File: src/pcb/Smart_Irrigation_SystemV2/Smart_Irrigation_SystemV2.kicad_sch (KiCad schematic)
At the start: 133 parts, among them CN1 PJ-3136-3A, CN2 PJ-3136-3A, CN3 PJ-3136-3A, CN4 PJ-3136-3A, CN5 PJ-3136-3A, CN6 PJ-3136-3A, J1 USB_C_Receptacle_USB2.0_16P, J10 I2C, J11 I2C, J13 I2C, J14 SolarPanel, J15 I2C, J16 GPIO_Expander, J2 FPC_Connector, J6 I2C, J9 Battary Connection, Q1 MUN5211DW1, Q2 FDN340P, Q3 AO3400A, SW1 IO0 Switch, SW2 EN Switch, SW3 SW_Push, SW4 SW_Push, SW5 SW_Push, SW6 SW_Push, U1 CP2102N-Axx-xQFN28, U10 ADS1115IDGS, U11 PCA9536DP, U2 ESP32-WROOM-32, U3 ADS1115IDGS, U4 DS3231MZ, U5 TLV62568ADRL, U6 SN74LVC245APW, U7 TP4056-42-ESOP8, U8 TPS63001, U9 AT24CS32-SSHM

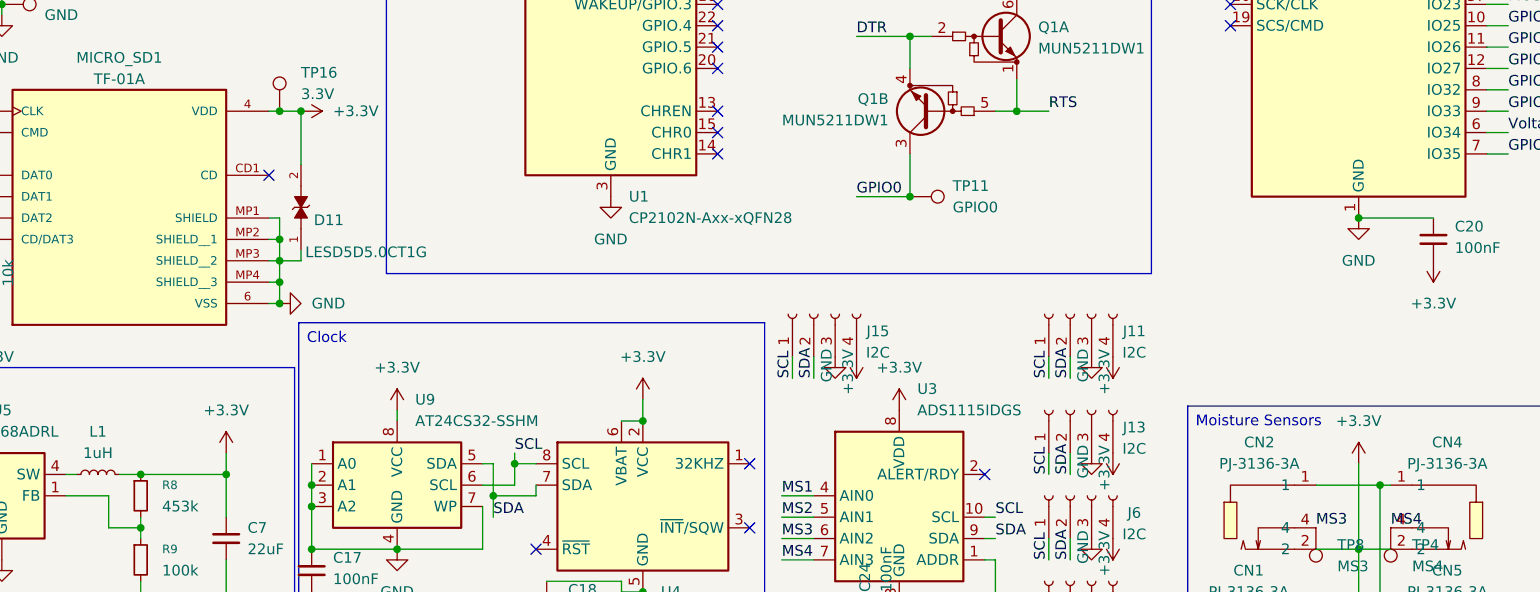
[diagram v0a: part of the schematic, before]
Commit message: solved warnings from drc and menaged silkscreen
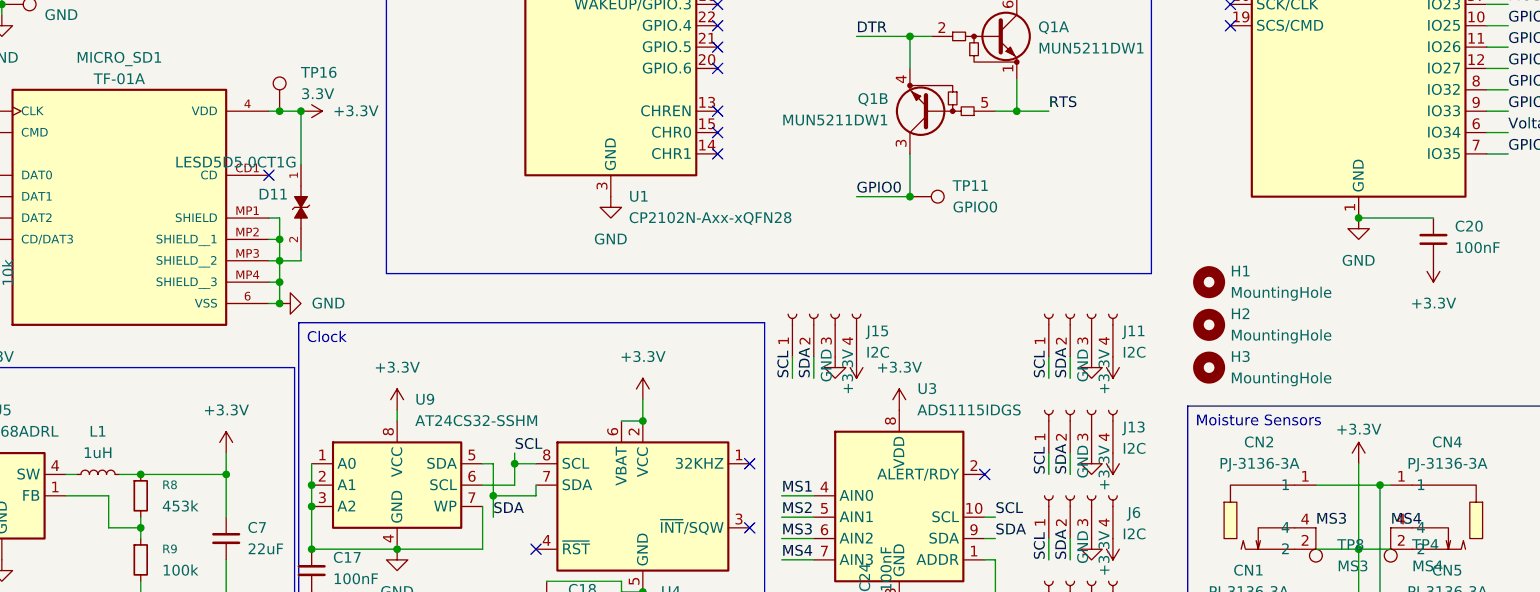
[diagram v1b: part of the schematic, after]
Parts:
- added H1, H2, H3: MountingHole, MountingHole:MountingHole_2.2mm_M2, symbol Mechanical:MountingHole
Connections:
- net +3.3V: now also D11.1; no longer D11.2
- net GND: now also D11.2; no longer D11.1
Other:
- moved on the sheet: D11
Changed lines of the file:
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@@
 	)
 	(symbol
+		(lib_id "Mechanical:MountingHole")
+		(at 173.99 96.52 0)
+		(unit 1)
+		(body_style 1)
+		(exclude_from_sim no)
+		(in_bom no)
+		(on_board yes)
+		(in_pos_files yes)
+		(dnp no)
+		(fields_autoplaced yes)
+		(property "Reference" "H1"
+			(at 176.53 95.2499 0)
+			(show_name no)
+			(do_not_autoplace no)
+			(effects
+				(font
+					(size 1.27 1.27)
+				)
+				(justify left)
+			)
+		)
+		(property "Value" "MountingHole"
+			(at 176.53 97.7899 0)
+			(show_name no)
+			(do_not_autoplace no)
+			(effects
+				(font
+					(size 1.27 1.27)
+				)
+				(justify left)
+			)
+		)
+		(property "Footprint" "MountingHole:MountingHole_2.2mm_M2"
+			(at 173.99 96.52 0)
+			(hide yes)
+			(show_name no)
+			(do_not_autoplace no)
+			(effects
+				(font
+					(size 1.27 1.27)
+				)
+			)
+		)
+		(property "Datasheet" ""
+			(at 173.99 96.52 0)
+			(hide yes)
+			(show_name no)
+			(do_not_autoplace no)
+			(effects
+				(font
+					(size 1.27 1.27)
+				)
+			)
+		)
+		(property "Description" "Mounting Hole without connection"
+			(at 173.99 96.52 0)
+			(hide yes)
+			(show_name no)
+			(do_not_autoplace no)
+			(effects
+				(font
+					(size 1.27 1.27)
+				)
+			)
+		)
+		(instances
+			(project "Smart_Irrigation_SystemV2"
+				(path "/53cd4412-b596-463c-8d76-f5cd1a4639a9"
+					(reference "H1")
+					(unit 1)
+				)
+			)
+		)
+	)
+	(symbol
 		(lib_id "Device:C_Small")
 		(at 208.28 171.45 0)
@@
 	(symbol
 		(lib_id "LESD5D5.0CT1G:LESD5D5.0CT1G")
-		(at 66.04 87.63 270)
+		(at 66.04 87.63 90)
 		(mirror x)
 		(unit 1)
@@
 		(dnp no)
 		(property "Reference" "D11"
-			(at 67.564 89.154 90)
+			(at 64.516 86.106 90)
 			(show_name no)
 			(do_not_autoplace no)
@@
 		)
 		(property "Value" "LESD5D5.0CT1G"
-			(at 66.548 92.964 90)
+			(at 65.532 82.296 90)
 			(show_name no)
 			(do_not_autoplace no)
@@
 		(in_pos_files yes)
 		(dnp no)
-		(fields_autoplaced yes)
 		(property "Reference" "#PWR069"
 			(at 191.77 121.92 0)
@@
 		)
 		(property "Value" "+3.3V"
-			(at 191.77 113.03 0)
+			(at 191.77 114.046 0)
 			(show_name no)
 			(do_not_autoplace no)
@@
 	)
 	(symbol
+		(lib_id "Mechanical:MountingHole")
+		(at 173.99 106.68 0)
+		(unit 1)
+		(body_style 1)
+		(exclude_from_sim no)
+		(in_bom no)
+		(on_board yes)
+		(in_pos_files yes)
+		(dnp no)
+		(fields_autoplaced yes)
+		(property "Reference" "H3"
+			(at 176.53 105.4099 0)
+			(show_name no)
+			(do_not_autoplace no)
+			(effects
+				(font
+					(size 1.27 1.27)
+				)
+				(justify left)
+			)
+		)
+		(property "Value" "MountingHole"
+			(at 176.53 107.9499 0)
+			(show_name no)
+			(do_not_autoplace no)
+			(effects
+				(font
+					(size 1.27 1.27)
+				)
+				(justify left)
+			)
+		)
+		(property "Footprint" "MountingHole:MountingHole_2.2mm_M2"
+			(at 173.99 106.68 0)
+			(hide yes)
+			(show_name no)
+			(do_not_autoplace no)
+			(effects
+				(font
+					(size 1.27 1.27)
+				)
+			)
+		)
+		(property "Datasheet" ""
+			(at 173.99 106.68 0)
+			(hide yes)
+			(show_name no)
+			(do_not_autoplace no)
+			(effects
+				(font
+					(size 1.27 1.27)
+				)
+			)
+		)
+		(property "Description" "Mounting Hole without connection"
+			(at 173.99 106.68 0)
+			(hide yes)
+			(show_name no)
+			(do_not_autoplace no)
+			(effects
+				(font
+					(size 1.27 1.27)
+				)
+			)
+		)
+		(instances
+			(project "Smart_Irrigation_SystemV2"
+				(path "/53cd4412-b596-463c-8d76-f5cd1a4639a9"
+					(reference "H3")
+					(unit 1)
+				)
+			)
+		)
+	)
+	(symbol
 		(lib_id "Device:R_Small")
 		(at 238.76 46.99 180)
@@
 					(unit 1)
 				)
+			)
+		)
+	)
+	(symbol
+		(lib_id "Mechanical:MountingHole")
+		(at 173.99 101.6 0)
+		(unit 1)
+		(body_style 1)
+		(exclude_from_sim no)
+		(in_bom no)
+		(on_board yes)
+		(in_pos_files yes)
+		(dnp no)
+		(fields_autoplaced yes)
+		(property "Reference" "H2"
+			(at 176.53 100.3299 0)
+			(show_name no)
+			(do_not_autoplace no)
+			(effects
+				(font
+					(size 1.27 1.27)
+				)
+				(justify left)
+			)
+		)
+		(property "Value" "MountingHole"
+			(at 176.53 102.8699 0)
+			(show_name no)
+			(do_not_autoplace no)
+			(effects
+				(font
+					(size 1.27 1.27)
+				)
+				(justify left)
+			)
+		)
+		(property "Footprint" "MountingHole:MountingHole_2.2mm_M2"
+			(at 173.99 101.6 0)
+			(hide yes)
+			(show_name no)
+			(do_not_autoplace no)
+			(effects
+				(font
+					(size 1.27 1.27)
+				)
+			)
+		)
+		(property "Datasheet" ""
+			(at 173.99 101.6 0)
+			(hide yes)
+			(show_name no)
+			(do_not_autoplace no)
+			(effects
+				(font
+					(size 1.27 1.27)
+				)
+			)
+		)
+		(property "Description" "Mounting Hole without connection"
+			(at 173.99 101.6 0)
+			(hide yes)
+			(show_name no)
+			(do_not_autoplace no)
+			(effects
+				(font
+					(size 1.27 1.27)
+				)
+			)
+		)
+		(instances
+			(project "Smart_Irrigation_SystemV2"
+				(path "/53cd4412-b596-463c-8d76-f5cd1a4639a9"
+					(reference "H2")
+					(unit 1)
+				)

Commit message: first gerber files, last polish
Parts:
- CN1, CN2, CN3, CN4, CN5, CN6: JLCPCB Part Number (none) -> C707248
- D10: JLCPCB Part Number C5355496 -> C513277
- U8: footprint C28060:VSON-10_L3.0-W3.0-P0.50-TL-EP_TPS62410DRCR -> Package_TO_SOT_SMD:SOT-23-5
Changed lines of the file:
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@@
 			)
 		)
+		(property "JLCPCB Part Number" "C707248"
+			(at 181.61 153.67 0)
+			(hide yes)
+			(show_name no)
+			(do_not_autoplace no)
+			(effects
+				(font
+					(size 1.27 1.27)
+				)
+			)
+		)
 		(pin "1"
 		)
@@
 			)
 		)
+		(property "JLCPCB Part Number" "C707248"
+			(at 200.66 138.43 0)
+			(hide yes)
+			(show_name no)
+			(do_not_autoplace no)
+			(effects
+				(font
+					(size 1.27 1.27)
+				)
+			)
+		)
 		(pin "1"
 		)
@@
 			)
 		)
+		(property "JLCPCB Part Number" "C707248"
+			(at 181.61 123.19 0)
+			(hide yes)
+			(show_name no)
+			(do_not_autoplace no)
+			(effects
+				(font
+					(size 1.27 1.27)
+				)
+			)
+		)
 		(pin "1"
 		)
@@
 			)
 		)
+		(property "JLCPCB Part Number" "C707248"
+			(at 200.66 123.19 0)
+			(hide yes)
+			(show_name no)
+			(do_not_autoplace no)
+			(effects
+				(font
+					(size 1.27 1.27)
+				)
+			)
+		)
 		(pin "1"
 		)
@@
 			)
 		)
+		(property "JLCPCB Part Number" "C707248"
+			(at 200.66 153.67 0)
+			(hide yes)
+			(show_name no)
+			(do_not_autoplace no)
+			(effects
+				(font
+					(size 1.27 1.27)
+				)
+			)
+		)
 		(pin "1"
 		)
@@
 			)
 		)
-		(property "JLCPCB Part Number" "C5355496"
+		(property "JLCPCB Part Number" "C513277"
 			(at 109.22 170.18 90)
 			(hide yes)
@@
 			)
 		)
-		(property "Footprint" "C28060:VSON-10_L3.0-W3.0-P0.50-TL-EP_TPS62410DRCR"
+		(property "Footprint" "Package_TO_SOT_SMD:SOT-23-5"
 			(at 157.48 190.5 0)
 			(hide yes)
@@
 			(hide yes)
 			(show_name no)
+			(do_not_autoplace no)
+			(effects
+				(font
+					(size 1.27 1.27)
+				)
+			)
+		)
+		(property "JLCPCB Part Number" "C707248"
+			(at 180.34 138.43 0)
+			(hide yes)
+			(show_name no)

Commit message: production ready!
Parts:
- removed C17: 100nF, Capacitor_SMD:C_0805_2012Metric, symbol Device:C_Small
- removed U9: AT24CS32-SSHM, Package_SO:SOIC-8_3.9x4.9mm_P1.27mm, symbol Memory_EEPROM:AT24CS32-SSHM
- SW3, SW4, SW5, SW6: footprint Button_Switch_THT:SW_PUSH_6mm_H4.3mm -> C83206:KEY-SMD_4P-L6.0-W6.0-P3.90-LS9.0; JLCPCB Part Number (none) -> C83206
- U5: footprint Package_TO_SOT_SMD:SOT-563 -> Package_TO_SOT_SMD:SOT-23-5
- U8: footprint Package_TO_SOT_SMD:SOT-23-5 -> Package_SON:VSON-10-1EP_3x3mm_P0.5mm_EP1.65x2.4mm_ThermalVias
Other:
- moved on the sheet: C18, J15, U4
